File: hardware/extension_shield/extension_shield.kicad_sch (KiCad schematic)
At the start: 12 parts

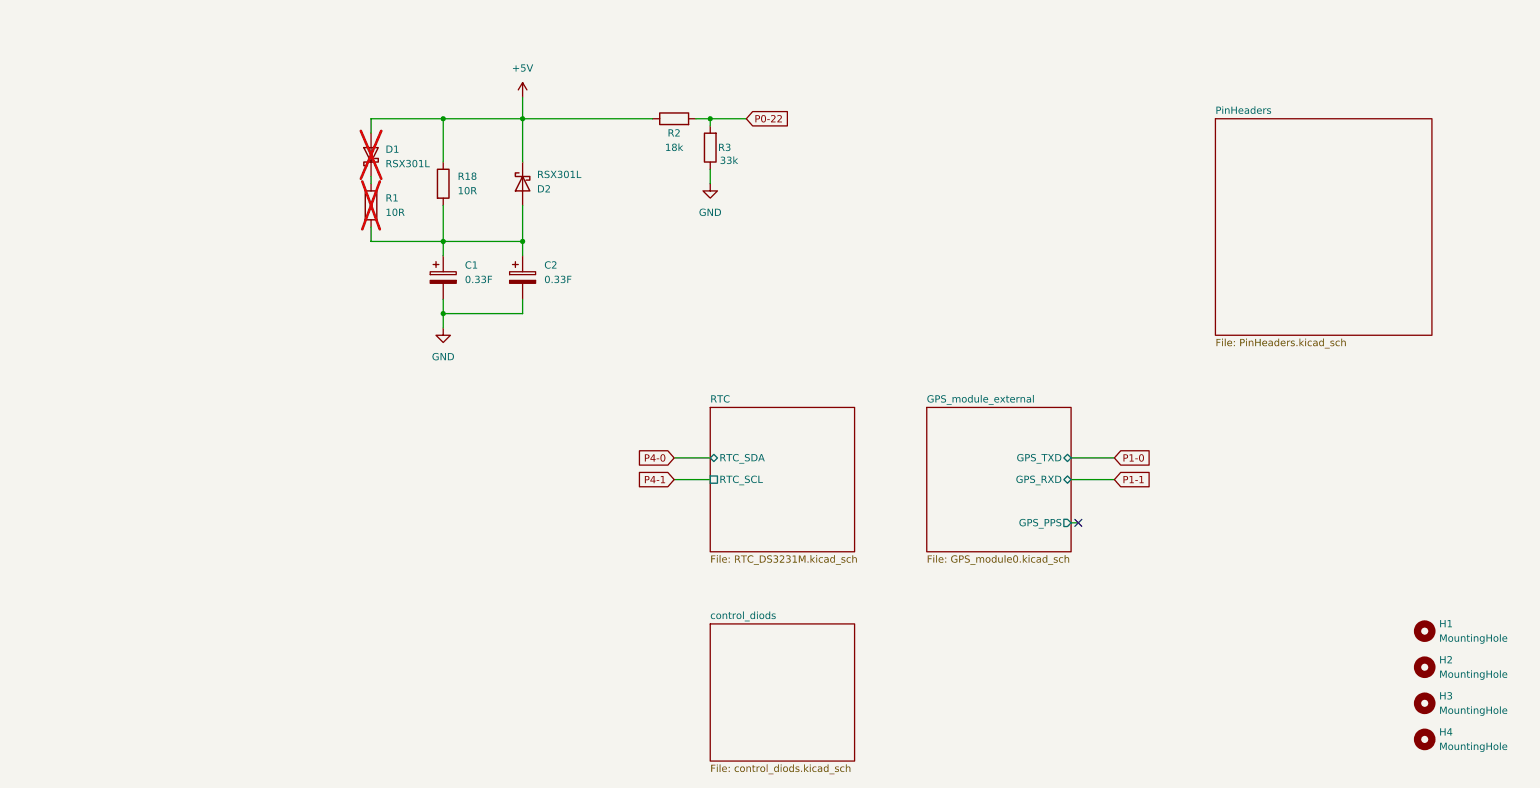
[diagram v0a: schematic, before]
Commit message: [HW] Adds Labels To Expansion Shield Schematic, PDF Schematic & Performed Schematic, PCB Tests.
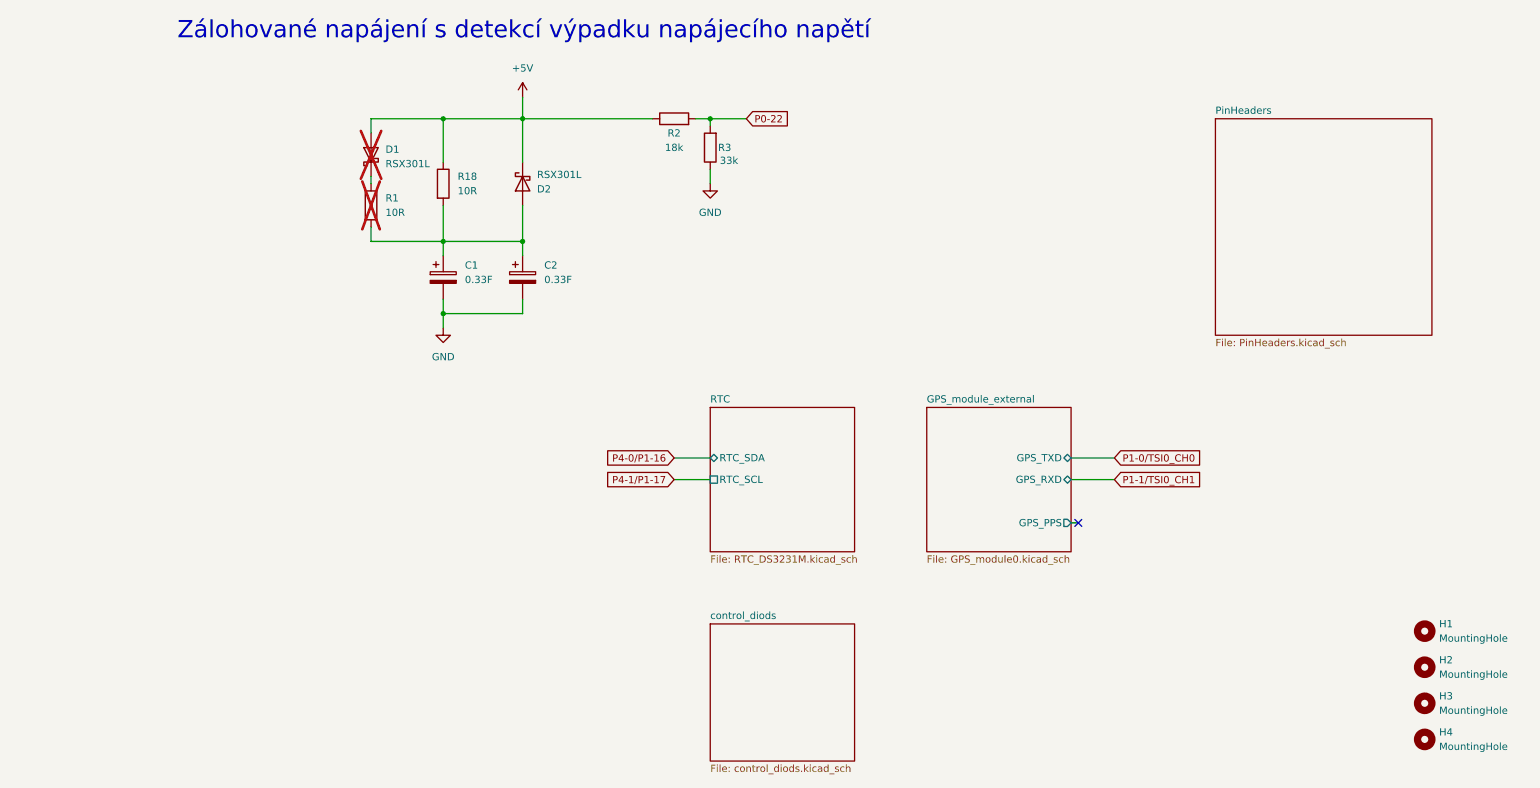
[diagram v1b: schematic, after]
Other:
- note added: "Zálohované napájení s detekcí výpadku napájecího napětí"
- title: Datalogger Expansion Shield -> Data Logger Expansion Shield
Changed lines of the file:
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@@
 	(paper "A4")
 	(title_block
-		(title "Datalogger Expansion Shield")
+		(title "Data Logger Expansion Shield")
 		(date "2025-02-26")
 		(rev "1.2")
@@
 		)
 	)
-	(global_label "P1-0"
+	(text "Zálohované napájení s detekcí výpadku napájecího napětí"
+		(exclude_from_sim no)
+		(at 94.234 22.606 0)
+		(effects
+			(font
+				(size 3.048 3.048)
+			)
+		)
+	)
+	(global_label "P1-0{slash}TSI0_CH0"
 		(shape input)
 		(at 198.12 97.79 0)
@@
 		)
 		(property "Intersheetrefs" "${INTERSHEET_REFS}"
-			(at 206.3666 97.79 0)
+			(at 216.4661 97.79 0)
 			(effects
 				(font
@@
 		)
 	)
-	(global_label "P4-1"
+	(global_label "P4-1{slash}P1-17"
 		(shape input)
 		(at 120.65 101.6 180)
@@
 		)
 		(property "Intersheetrefs" "${INTERSHEET_REFS}"
-			(at 112.4034 101.6 0)
+			(at 99.2197 101.6 0)
 			(effects
 				(font
@@
 		)
 	)
-	(global_label "P4-0"
+	(global_label "P4-0{slash}P1-16"
 		(shape input)
 		(at 120.65 97.79 180)
@@
 		)
 		(property "Intersheetrefs" "${INTERSHEET_REFS}"
-			(at 112.4034 97.79 0)
+			(at 99.2197 97.79 0)
 			(effects
 				(font
@@
 		)
 	)
-	(global_label "P1-1"
+	(global_label "P1-1{slash}TSI0_CH1"
 		(shape input)
 		(at 198.12 101.6 0)
@@
 		)
 		(property "Intersheetrefs" "${INTERSHEET_REFS}"
-			(at 206.3666 101.6 0)
+			(at 216.4661 101.6 0)
 			(effects
 				(font
